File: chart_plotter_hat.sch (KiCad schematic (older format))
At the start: 38 parts, among them J1 Conn_02x03_Odd_Even, J2 Conn_01x04, J3 40HAT, J4 Conn_01x04, J5 Conn_01x04, J6 Conn_01x02, J7 Conn_01x04, J8 Conn_02x03_Odd_Even, Q1 DMG2305UX, Q2 DMMT5401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

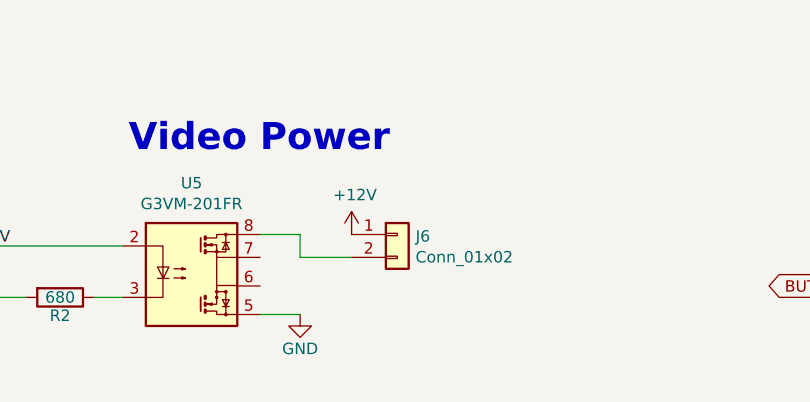
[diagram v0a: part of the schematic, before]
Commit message: Redid relay wiring
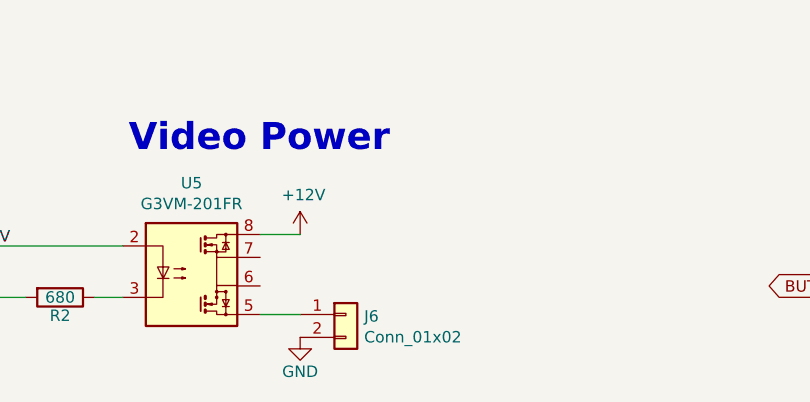
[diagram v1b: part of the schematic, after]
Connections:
- net +12V: now also U5.8; no longer J6.1 (Pin_1)
- net GND: now also J6.2 (Pin_2); no longer U5.5
- new net: J6.1 (Pin_1), U5.5
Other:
- moved on the sheet: J6
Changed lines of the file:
@@
 L Connector_Generic:Conn_01x02 J6
 U 1 1 5FEFCBF8
-P 6350 10075
-F 0 "J6" H 6430 10067 50  0000 L CNN
-F 1 "Conn_01x02" H 6430 9976 50  0000 L CNN
-F 2 "Connectors_JST:JST_PH_B2B-PH-K_02x2.00mm_Straight" H 6350 10075 50  0001 C CNN
-F 3 "~" H 6350 10075 50  0001 C CNN
-	1    6350 10075
+P 6125 10425
+F 0 "J6" H 6205 10417 50  0000 L CNN
+F 1 "Conn_01x02" H 6205 10326 50  0000 L CNN
+F 2 "Connectors_JST:JST_PH_B2B-PH-K_02x2.00mm_Straight" H 6125 10425 50  0001 C CNN
+F 3 "~" H 6125 10425 50  0001 C CNN
+	1    6125 10425
 	1    0    0    -1
 $EndComp
 Text Notes 5175 9725 0    118  ~ 24
 Video Power
-$Comp
-L power:+12V #PWR0112
-U 1 1 5FF1CC91
-P 6150 10075
-F 0 "#PWR0112" H 6150 9925 50  0001 C CNN
-F 1 "+12V" H 6165 10248 50  0000 C CNN
-F 2 "" H 6150 10075 50  0001 C CNN
-F 3 "" H 6150 10075 50  0001 C CNN
-	1    6150 10075
-	1    0    0    -1
-$EndComp
 $Comp
 L power:GND #PWR0113
@@
 $EndComp
 Wire Wire Line
-	6150 10175 5925 10175
-Wire Wire Line
-	5925 10175 5925 10075
-Wire Wire Line
 	5925 10075 5750 10075
 Wire Wire Line
 	5750 10425 5925 10425
-$Comp
-L power:GND #PWR0118
-U 1 1 5FF48764
-P 5925 10425
-F 0 "#PWR0118" H 5925 10175 50  0001 C CNN
-F 1 "GND" H 5925 10275 50  0000 C CNN
-F 2 "" H 5925 10425 50  0000 C CNN
-F 3 "" H 5925 10425 50  0000 C CNN
-	1    5925 10425
-	1    0    0    -1
-$EndComp
 Wire Wire Line
 	5025 10350 5150 10350
@@
 Wire Wire Line
 	13125 6000 13325 6000
+$Comp
+L power:+12V #PWR?
+U 1 1 5FF248A7
+P 5925 10075
+F 0 "#PWR?" H 5925 9925 50  0001 C CNN
+F 1 "+12V" H 5940 10248 50  0000 C CNN
+F 2 "" H 5925 10075 50  0001 C CNN
+F 3 "" H 5925 10075 50  0001 C CNN
+	1    5925 10075
+	1    0    0    -1
+$EndComp
+$Comp
+L power:GND #PWR?
+U 1 1 5FF24DFF
+P 5925 10525
+F 0 "#PWR?" H 5925 10275 50  0001 C CNN
+F 1 "GND" H 5925 10375 50  0000 C CNN
+F 2 "" H 5925 10525 50  0000 C CNN
+F 3 "" H 5925 10525 50  0000 C CNN
+	1    5925 10525
+	1    0    0    -1
+$EndComp
 $EndSCHEMATC

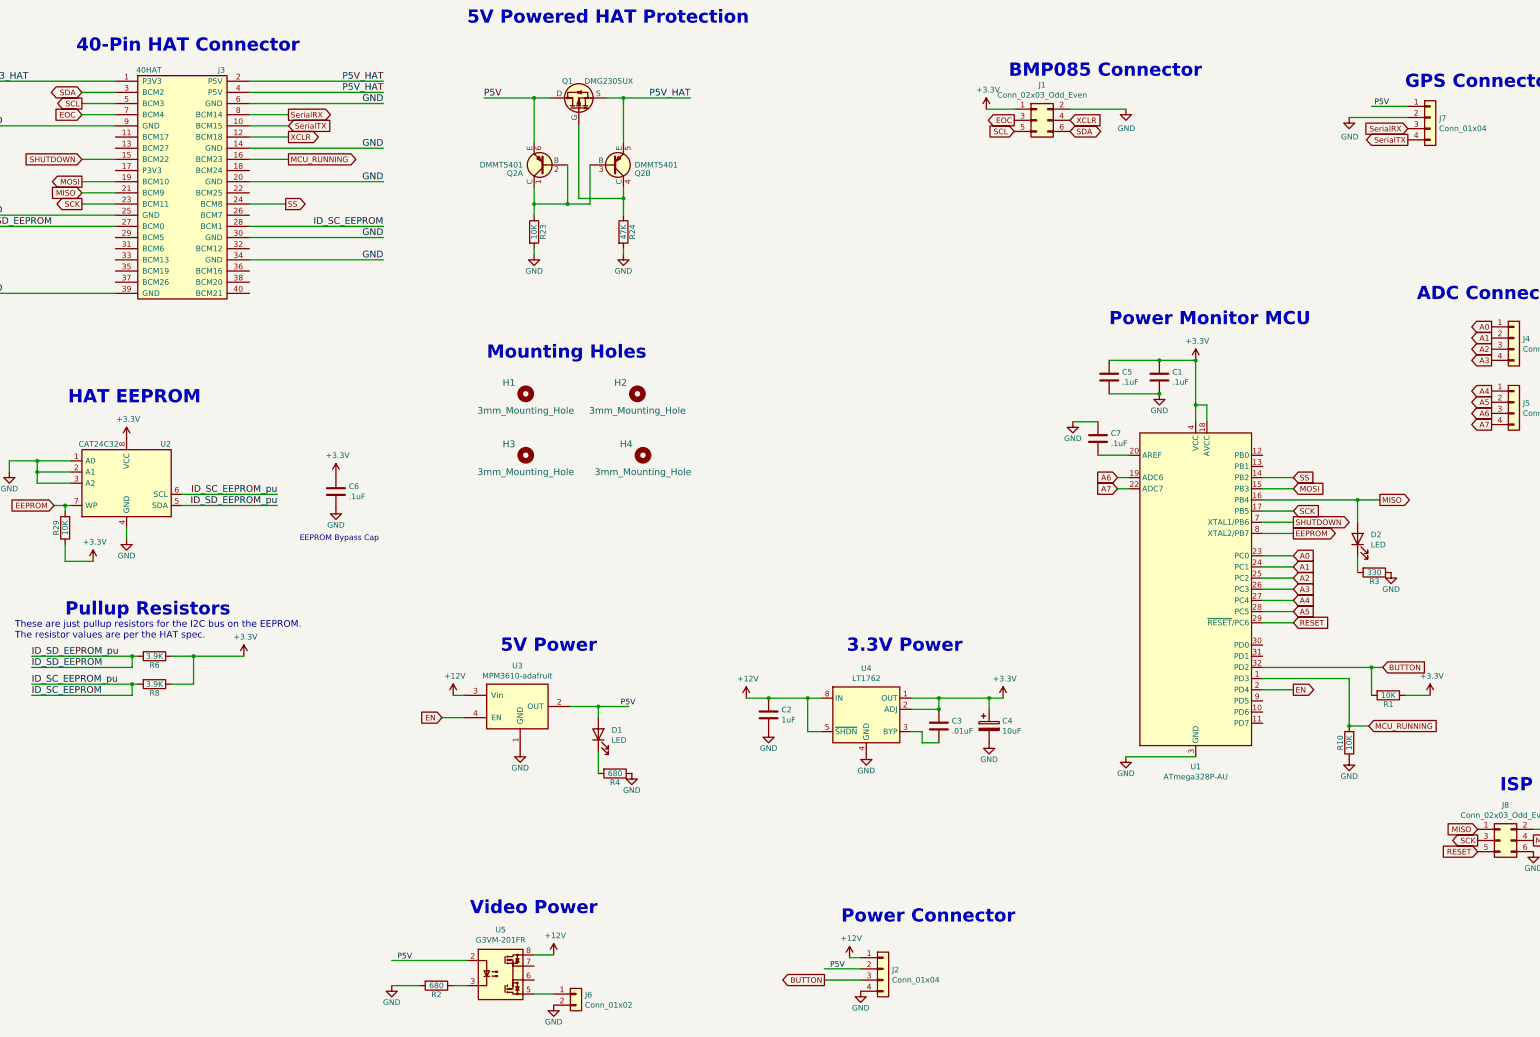
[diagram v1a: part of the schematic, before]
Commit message: Added voltmeter connection
Added reverse polarity protection diode
Moved non-power LED to it's own pin
Added R5, SHUTDOWN pull-down resistor
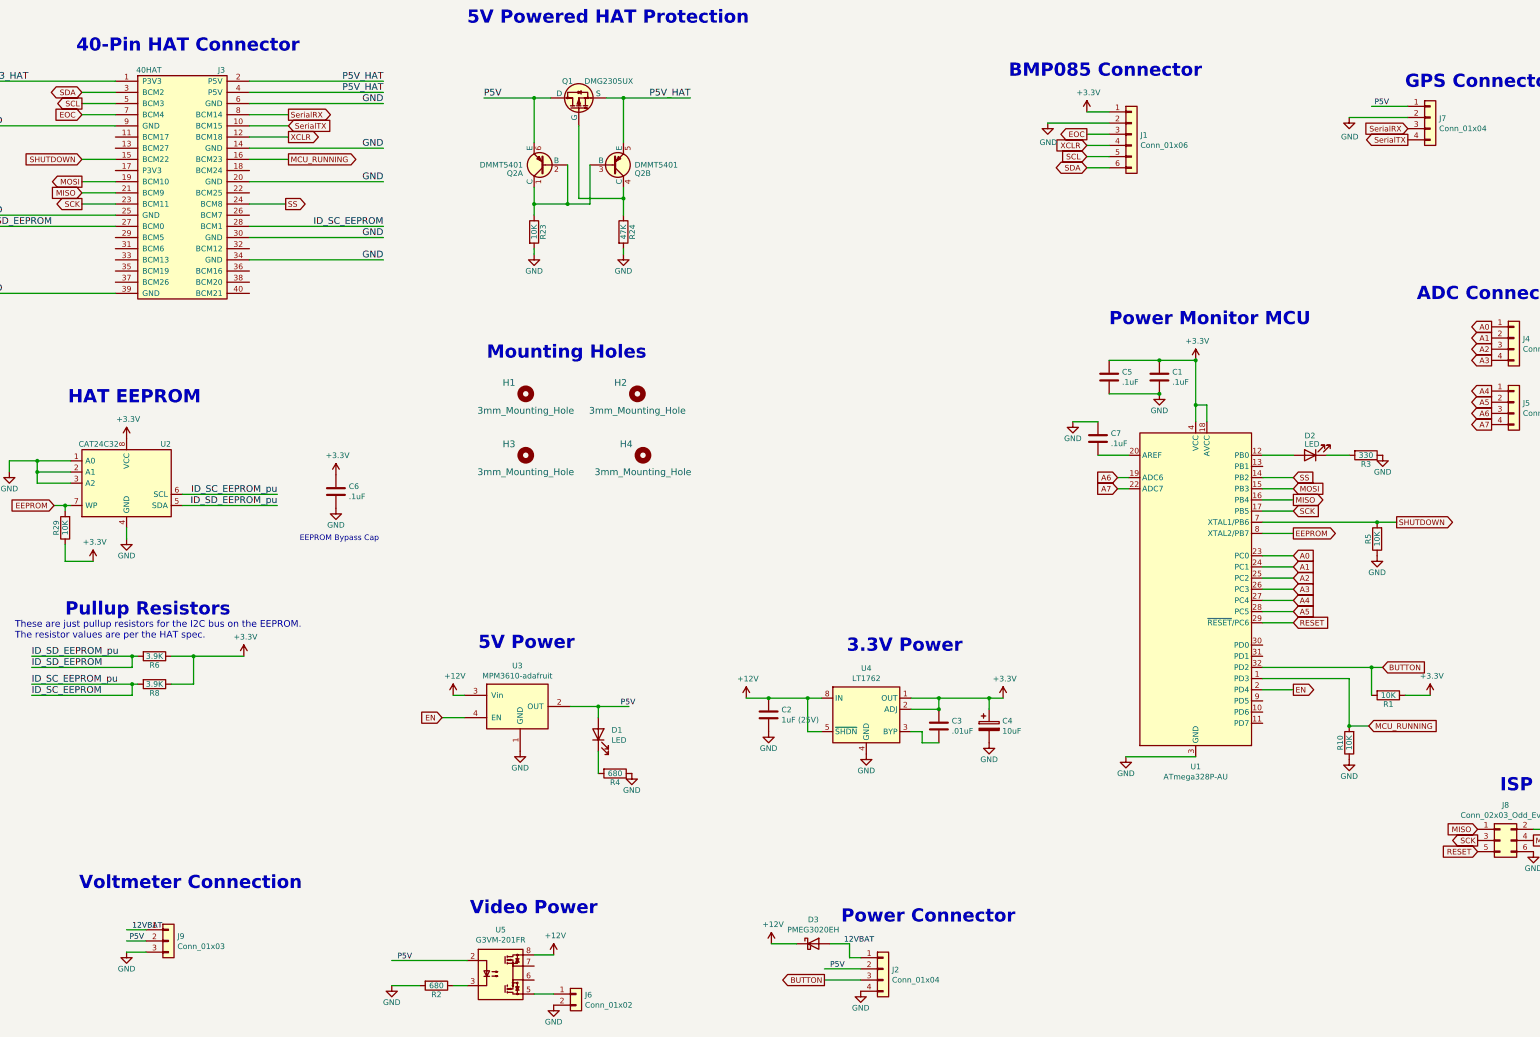
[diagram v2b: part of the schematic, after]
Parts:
- removed J1: Conn_02x03_Odd_Even, CustomComponents:BOX-HEADER6, symbol Connector_Generic:Conn_02x03_Odd_Even
- added D3: PMEG3020EH, Diodes_SMD:D_SOD-123, symbol Diode:PMEG3020EH
- added J1: Conn_01x06, Connectors_JST:JST_PH_B6B-PH-K_06x2.00mm_Straight, symbol Connector_Generic:Conn_01x06
- added J9: Conn_01x03, Connectors_JST:JST_PH_B3B-PH-K_03x2.00mm_Straight, symbol Connector_Generic:Conn_01x03
- added R5: 10K, Resistors_SMD:R_0603, symbol Device:R
- C2: value 1uF -> 1uF (25V)
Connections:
- net labels added: 12VBAT
- wire segments 139 -> 149
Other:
- note added: "Voltmeter Connection"
- moved on the sheet: D2, R3
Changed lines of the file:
@@
 Wire Wire Line
 	1550 6050 1550 6100
-$Comp
-L Connector_Generic:Conn_02x03_Odd_Even J1
-U 1 1 5FD37EF3
-P 10250 2600
-F 0 "J1" H 10300 2917 50  0000 C CNN
-F 1 "Conn_02x03_Odd_Even" H 10300 2826 50  0000 C CNN
-F 2 "CustomComponents:BOX-HEADER6" H 10250 2600 50  0001 C CNN
-F 3 "~" H 10250 2600 50  0001 C CNN
-	1    10250 2600
-	1    0    0    -1
-$EndComp
 Text Notes 10000 2225 0    118  ~ 24
 BMP085 Connector
@@
 L power:GND #PWR0108
 U 1 1 5FDC841D
-P 11050 2500
-F 0 "#PWR0108" H 11050 2250 50  0001 C CNN
-F 1 "GND" H 11055 2327 50  0000 C CNN
-F 2 "" H 11050 2500 50  0001 C CNN
-F 3 "" H 11050 2500 50  0001 C CNN
-	1    11050 2500
-	1    0    0    -1
-$EndComp
-Wire Wire Line
-	10550 2500 11050 2500
-Text GLabel 10550 2600 2    50   Input ~ 0
+P 10350 2625
+F 0 "#PWR0108" H 10350 2375 50  0001 C CNN
+F 1 "GND" H 10355 2452 50  0000 C CNN
+F 2 "" H 10350 2625 50  0001 C CNN
+F 3 "" H 10350 2625 50  0001 C CNN
+	1    10350 2625
+	1    0    0    -1
+$EndComp
+Text GLabel 10700 2825 0    50   Input ~ 0
 XCLR
-Text GLabel 10550 2700 2    50   BiDi ~ 0
+Text GLabel 10700 3025 0    50   BiDi ~ 0
 SDA
-Text GLabel 10050 2700 0    50   Input ~ 0
+Text GLabel 10700 2925 0    50   Input ~ 0
 SCL
-Text GLabel 10050 2600 0    50   Output ~ 0
+Text GLabel 10700 2725 0    50   Output ~ 0
 EOC
-Wire Wire Line
-	10050 2500 9800 2500
 Text Notes 8500 9800 0    118  ~ 24
 Power Connector
@@
 Text GLabel 12550 6100 2    50   Input ~ 0
 SCK
-Text GLabel 13325 6000 2    50   Output ~ 0
+Text GLabel 12550 6000 2    50   Output ~ 0
 MISO
 Text GLabel 12550 5900 2    50   Input ~ 0
@@
 	1    0    0    -1
 $EndComp
-Text GLabel 12550 6200 2    50   Output ~ 0
+Text GLabel 13475 6200 2    50   Output ~ 0
 SHUTDOWN
 Text GLabel 13225 8025 2    50   Input ~ 0
@@
 P 7850 7925
 F 0 "C2" H 7965 7971 50  0000 L CNN
-F 1 "1uF" H 7965 7880 50  0000 L CNN
+F 1 "1uF (25V)" H 7965 7880 50  0000 L CNN
 F 2 "Capacitors_SMD:C_1206" H 7888 7775 50  0001 C CNN
 F 3 "~" H 7850 7925 50  0001 C CNN
@@
 	2000 2950 1700 2950
 $Comp
-L power:+3.3V #PWR0109
-U 1 1 5FE11920
-P 9800 2500
-F 0 "#PWR0109" H 9800 2350 50  0001 C CNN
-F 1 "+3.3V" H 9815 2673 50  0000 C CNN
-F 2 "" H 9800 2500 50  0001 C CNN
-F 3 "" H 9800 2500 50  0001 C CNN
-	1    9800 2500
-	1    0    0    -1
-$EndComp
-$Comp
 L power:+3.3V #PWR0110
 U 1 1 5FE2CEAF
@@
 L Device:LED D2
 U 1 1 5FFED207
-P 13125 6350
-F 0 "D2" V 13164 6232 50  0000 R CNN
-F 1 "LED" V 13073 6232 50  0000 R CNN
-F 2 "LEDs:LED_0603" H 13125 6350 50  0001 C CNN
-F 3 "~" H 13125 6350 50  0001 C CNN
-	1    13125 6350
-	0    -1   -1   0
+P 12700 5600
+F 0 "D2" H 12750 5425 50  0000 R CNN
+F 1 "LED" H 12750 5500 50  0000 R CNN
+F 2 "LEDs:LED_0603" H 12700 5600 50  0001 C CNN
+F 3 "~" H 12700 5600 50  0001 C CNN
+	1    12700 5600
+	-1   0    0    1
 $EndComp
 $Comp
 L Device:R R3
 U 1 1 5FFED8DA
-P 13275 6650
-F 0 "R3" V 13355 6650 50  0000 C CNN
-F 1 "330" V 13275 6650 50  0000 C CNN
-F 2 "Resistors_SMD:R_0603" V 13205 6650 50  0001 C CNN
-F 3 "" H 13275 6650 50  0001 C CNN
-	1    13275 6650
+P 13200 5600
+F 0 "R3" V 13280 5600 50  0000 C CNN
+F 1 "330" V 13200 5600 50  0000 C CNN
+F 2 "Resistors_SMD:R_0603" V 13130 5600 50  0001 C CNN
+F 3 "" H 13200 5600 50  0001 C CNN
+	1    13200 5600
 	0    1    1    0
 $EndComp
@@
 L power:GND #PWR017
 U 1 1 600009B4
-P 13425 6650
-F 0 "#PWR017" H 13425 6400 50  0001 C CNN
-F 1 "GND" H 13425 6500 50  0000 C CNN
-F 2 "" H 13425 6650 50  0000 C CNN
-F 3 "" H 13425 6650 50  0000 C CNN
-	1    13425 6650
+P 13350 5600
+F 0 "#PWR017" H 13350 5350 50  0001 C CNN
+F 1 "GND" H 13350 5450 50  0000 C CNN
+F 2 "" H 13350 5600 50  0000 C CNN
+F 3 "" H 13350 5600 50  0000 C CNN
+	1    13350 5600
 	1    0    0    -1
 $EndComp
@@
 L power:+12V #PWR0101
 U 1 1 5FE250C0
-P 8575 10100
-F 0 "#PWR0101" H 8575 9950 50  0001 C CNN
-F 1 "+12V" H 8590 10273 50  0000 C CNN
-F 2 "" H 8575 10100 50  0001 C CNN
-F 3 "" H 8575 10100 50  0001 C CNN
-	1    8575 10100
+P 7875 9975
+F 0 "#PWR0101" H 7875 9825 50  0001 C CNN
+F 1 "+12V" H 7890 10148 50  0000 C CNN
+F 2 "" H 7875 9975 50  0001 C CNN
+F 3 "" H 7875 9975 50  0001 C CNN
+	1    7875 9975
 	1    0    0    -1
 $EndComp
@@
 Text Notes 8550 7375 0    118  ~ 24
 3.3V Power
-Text Notes 5450 7375 0    118  ~ 24
+Text Notes 5250 7350 0    118  ~ 24
 5V Power
 Text Notes 10900 4450 0    118  ~ 24
@@
 Wire Wire Line
 	4925 7950 5125 7950
-Wire Wire Line
-	13125 6500 13125 6650
 $Comp
 L CustomComponents:G3VM-201FR U5
@@
 Wire Wire Line
 	4475 10125 5150 10125
-Wire Wire Line
-	12275 6200 12550 6200
-Wire Wire Line
-	12275 6000 13125 6000
-Wire Wire Line
-	13125 6200 13125 6000
-Connection ~ 13125 6000
-Wire Wire Line
-	13125 6000 13325 6000
-$Comp
-L power:+12V #PWR?
+$Comp
+L power:+12V #PWR0109
 U 1 1 5FF248A7
 P 5925 10075
-F 0 "#PWR?" H 5925 9925 50  0001 C CNN
+F 0 "#PWR0109" H 5925 9925 50  0001 C CNN
 F 1 "+12V" H 5940 10248 50  0000 C CNN
 F 2 "" H 5925 10075 50  0001 C CNN
@@
 $EndComp
 $Comp
-L power:GND #PWR?
+L power:GND #PWR0112
 U 1 1 5FF24DFF
 P 5925 10525
-F 0 "#PWR?" H 5925 10275 50  0001 C CNN
+F 0 "#PWR0112" H 5925 10275 50  0001 C CNN
 F 1 "GND" H 5925 10375 50  0000 C CNN
 F 2 "" H 5925 10525 50  0000 C CNN
@@
 	1    0    0    -1
 $EndComp
+Text Notes 1675 9500 0    118  ~ 24
+Voltmeter Connection
+$Comp
+L power:+3.3V #PWR0118
+U 1 1 5FF94F7E
+P 10700 2525
+F 0 "#PWR0118" H 10700 2375 50  0001 C CNN
+F 1 "+3.3V" H 10715 2698 50  0000 C CNN
+F 2 "" H 10700 2525 50  0001 C CNN
+F 3 "" H 10700 2525 50  0001 C CNN
+	1    10700 2525
+	1    0    0    -1
+$EndComp
+$Comp
+L Connector_Generic:Conn_01x06 J1
+U 1 1 5FF9F71C
+P 11100 2725
+F 0 "J1" H 11180 2717 50  0000 L CNN
+F 1 "Conn_01x06" H 11180 2626 50  0000 L CNN
+F 2 "Connectors_JST:JST_PH_B6B-PH-K_06x2.00mm_Straight" H 11100 2725 50  0001 C CNN
+F 3 "~" H 11100 2725 50  0001 C CNN
+	1    11100 2725
+	1    0    0    -1
+$EndComp
+Wire Wire Line
+	10700 2525 10900 2525
+Wire Wire Line
+	10350 2625 10900 2625
+Wire Wire Line
+	10700 2725 10900 2725
+Wire Wire Line
+	10700 2825 10900 2825
+Wire Wire Line
+	10700 2925 10900 2925
+Wire Wire Line
+	10700 3025 10900 3025
+$Comp
+L Connector_Generic:Conn_01x03 J9
+U 1 1 5FF77E36
+P 2475 9950
+F 0 "J9" H 2555 9992 50  0000 L CNN
+F 1 "Conn_01x03" H 2555 9901 50  0000 L CNN
+F 2 "Connectors_JST:JST_PH_B3B-PH-K_03x2.00mm_Straight" H 2475 9950 50  0001 C CNN
+F 3 "~" H 2475 9950 50  0001 C CNN
+	1    2475 9950
+	1    0    0    -1
+$EndComp
+$Comp
+L power:GND #PWR0119
+U 1 1 600053DC
+P 2100 10050
+F 0 "#PWR0119" H 2100 9800 50  0001 C CNN
+F 1 "GND" H 2100 9900 50  0000 C CNN
+F 2 "" H 2100 10050 50  0000 C CNN
+F 3 "" H 2100 10050 50  0000 C CNN
+	1    2100 10050
+	1    0    0    -1
+$EndComp
+Wire Wire Line
+	2275 9850 2100 9850
+Wire Wire Line
+	2275 10050 2100 10050
+Wire Wire Line
+	8400 9975 8575 9975
+Wire Wire Line
+	8575 9975 8575 10100
+Wire Wire Line
+	8100 9975 7875 9975
+Text Label 8525 9975 0    50   ~ 0
+12VBAT
+Wire Wire Line
+	2275 9950 2100 9950
+Text Label 2125 9950 0    50   ~ 0
+P5V
+Text Label 2150 9850 0    50   ~ 0
+12VBAT
+Wire Wire Line
+	12275 6000 12550 6000
+Wire Wire Line
+	12275 5600 12550 5600
+Wire Wire Line
+	12850 5600 13050 5600
+$Comp
+L Device:R R5
+U 1 1 6013CE2D
+P 13300 6350
+F 0 "R5" V 13380 6350 50  0000 C CNN
+F 1 "10K" V 13300 6350 50  0000 C CNN
+F 2 "Resistors_SMD:R_0603" V 13230 6350 50  0001 C CNN
+F 3 "" H 13300 6350 50  0001 C CNN
+	1    13300 6350
+	-1   0    0    1
+$EndComp
+Wire Wire Line
+	12275 6200 13300 6200
+Connection ~ 13300 6200
+Wire Wire Line
+	13300 6200 13475 6200
+$Comp
+L power:GND #PWR04
+U 1 1 6014DAF4
+P 13300 6500
+F 0 "#PWR04" H 13300 6250 50  0001 C CNN
+F 1 "GND" H 13300 6350 50  0000 C CNN
+F 2 "" H 13300 6500 50  0000 C CNN
+F 3 "" H 13300 6500 50  0000 C CNN
+	1    13300 6500
+	1    0    0    -1
+$EndComp
+$Comp
+L Diode:PMEG3020EH D3
+U 1 1 6019111C
+P 8250 9975
+F 0 "D3" H 8250 10191 50  0000 C CNN
+F 1 "PMEG3020EH" H 8250 10100 50  0000 C CNN
+F 2 "Diodes_SMD:D_SOD-123" H 8250 9800 50  0001 C CNN
+F 3 "https://assets.nexperia.com/documents/data-sheet/PMEG3020EH_EJ.pdf" H 8250 9975 50  0001 C CNN
+	1    8250 9975
+	1    0    0    -1
+$EndComp
